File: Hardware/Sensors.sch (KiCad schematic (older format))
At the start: 8 parts, among them U4 MS5611, U5 HMC5883L, U6 L3G4200D

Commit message: Roughed out PCB layout
Known issues:
- SW_PUSH holes too small. New footprint needed
- Sensor footprints are completely wrong.
- Regulator footprints might not be correct.

Tasks:
- Place passives according to schematic (especially
  with decoupling capacitors.
- Condense layout as much as possible for
  smallest board size
- Route board
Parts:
- C15, C16, C3, C4: footprint (none) -> Capacitors_SMD:C_0805_HandSoldering
- R6: footprint (none) -> Resistors_SMD:R_0805_HandSoldering
- U4: footprint (none) -> SON:SON125P500X300-8N
- U5, U6: footprint (none) -> Housings_SSOP:SSOP-16_4.4x5.2mm_Pitch0.65mm
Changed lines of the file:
@@
 F 0 "U5" H 4050 3650 60  0000 C CNN
 F 1 "HMC5883L" H 4050 3450 60  0000 C CNN
-F 2 "" H 4200 3350 60  0000 C CNN
+F 2 "Housings_SSOP:SSOP-16_4.4x5.2mm_Pitch0.65mm" H 4200 3350 60  0001 C CNN
 F 3 "" H 4200 3350 60  0000 C CNN
 	1    4050 3550
@@
 F 0 "U4" H 2200 4000 60  0000 C CNN
 F 1 "MS5611" H 2200 3100 60  0000 C CNN
-F 2 "" H 2200 3850 60  0000 C CNN
+F 2 "SON:SON125P500X300-8N" H 2200 3850 60  0001 C CNN
 F 3 "" H 2200 3850 60  0000 C CNN
 	1    2200 3550
@@
 F 0 "U6" H 6900 3650 60  0000 C CNN
 F 1 "L3G4200D" H 6900 3450 60  0000 C CNN
-F 2 "" H 7050 3350 60  0000 C CNN
+F 2 "Housings_SSOP:SSOP-16_4.4x5.2mm_Pitch0.65mm" H 7050 3350 60  0001 C CNN
 F 3 "" H 7050 3350 60  0000 C CNN
 	1    6900 3550
@@
 F 0 "C4" H 4900 4200 50  0000 L CNN
 F 1 "4.6uF" H 4900 4000 50  0000 L CNN
-F 2 "" H 4888 3950 30  0000 C CNN
+F 2 "Capacitors_SMD:C_0805_HandSoldering" H 4888 3950 30  0001 C CNN
 F 3 "" H 4850 4100 60  0000 C CNN
 	1    4850 4100
@@
 F 0 "C3" H 4600 4200 50  0000 L CNN
 F 1 ".22uF" H 4600 4000 50  0000 L CNN
-F 2 "" H 4588 3950 30  0000 C CNN
+F 2 "Capacitors_SMD:C_0805_HandSoldering" H 4588 3950 30  0001 C CNN
 F 3 "" H 4550 4100 60  0000 C CNN
 	1    4550 4100
@@
 F 0 "C16" H 8600 2950 50  0000 L CNN
 F 1 ".47uF" H 8600 2750 50  0000 L CNN
-F 2 "" H 8588 2700 30  0000 C CNN
+F 2 "Capacitors_SMD:C_0805_HandSoldering" H 8588 2700 30  0001 C CNN
 F 3 "" H 8550 2850 60  0000 C CNN
 	1    8550 2850
@@
 F 0 "C15" H 8350 2550 50  0000 L CNN
 F 1 ".01uF" H 8350 2350 50  0000 L CNN
-F 2 "" H 8338 2300 30  0000 C CNN
+F 2 "Capacitors_SMD:C_0805_HandSoldering" H 8338 2300 30  0001 C CNN
 F 3 "" H 8300 2450 60  0000 C CNN
 	1    8300 2450
@@
 F 0 "R6" V 8130 2850 50  0000 C CNN
 F 1 "10K" V 8057 2851 50  0000 C CNN
-F 2 "" V 7980 2850 30  0000 C CNN
+F 2 "Resistors_SMD:R_0805_HandSoldering" V 7980 2850 30  0001 C CNN
 F 3 "" H 8050 2850 30  0000 C CNN
 	1    8050 2850

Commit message: Began routing
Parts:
- U5: footprint Housings_SSOP:SSOP-16_4.4x5.2mm_Pitch0.65mm -> PQFN:PQFN50P300X300-16N-EXTENDED
- U6: footprint Housings_SSOP:SSOP-16_4.4x5.2mm_Pitch0.65mm -> PQFN:PQFN65P400X400-16N-EXTENDED
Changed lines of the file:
@@
 F 0 "U5" H 4050 3650 60  0000 C CNN
 F 1 "HMC5883L" H 4050 3450 60  0000 C CNN
-F 2 "Housings_SSOP:SSOP-16_4.4x5.2mm_Pitch0.65mm" H 4200 3350 60  0001 C CNN
+F 2 "PQFN:PQFN50P300X300-16N-EXTENDED" H 4200 3350 60  0001 C CNN
 F 3 "" H 4200 3350 60  0000 C CNN
 	1    4050 3550
@@
 F 0 "U6" H 6900 3650 60  0000 C CNN
 F 1 "L3G4200D" H 6900 3450 60  0000 C CNN
-F 2 "Housings_SSOP:SSOP-16_4.4x5.2mm_Pitch0.65mm" H 7050 3350 60  0001 C CNN
+F 2 "PQFN:PQFN65P400X400-16N-EXTENDED" H 7050 3350 60  0001 C CNN
 F 3 "" H 7050 3350 60  0000 C CNN
 	1    6900 3550

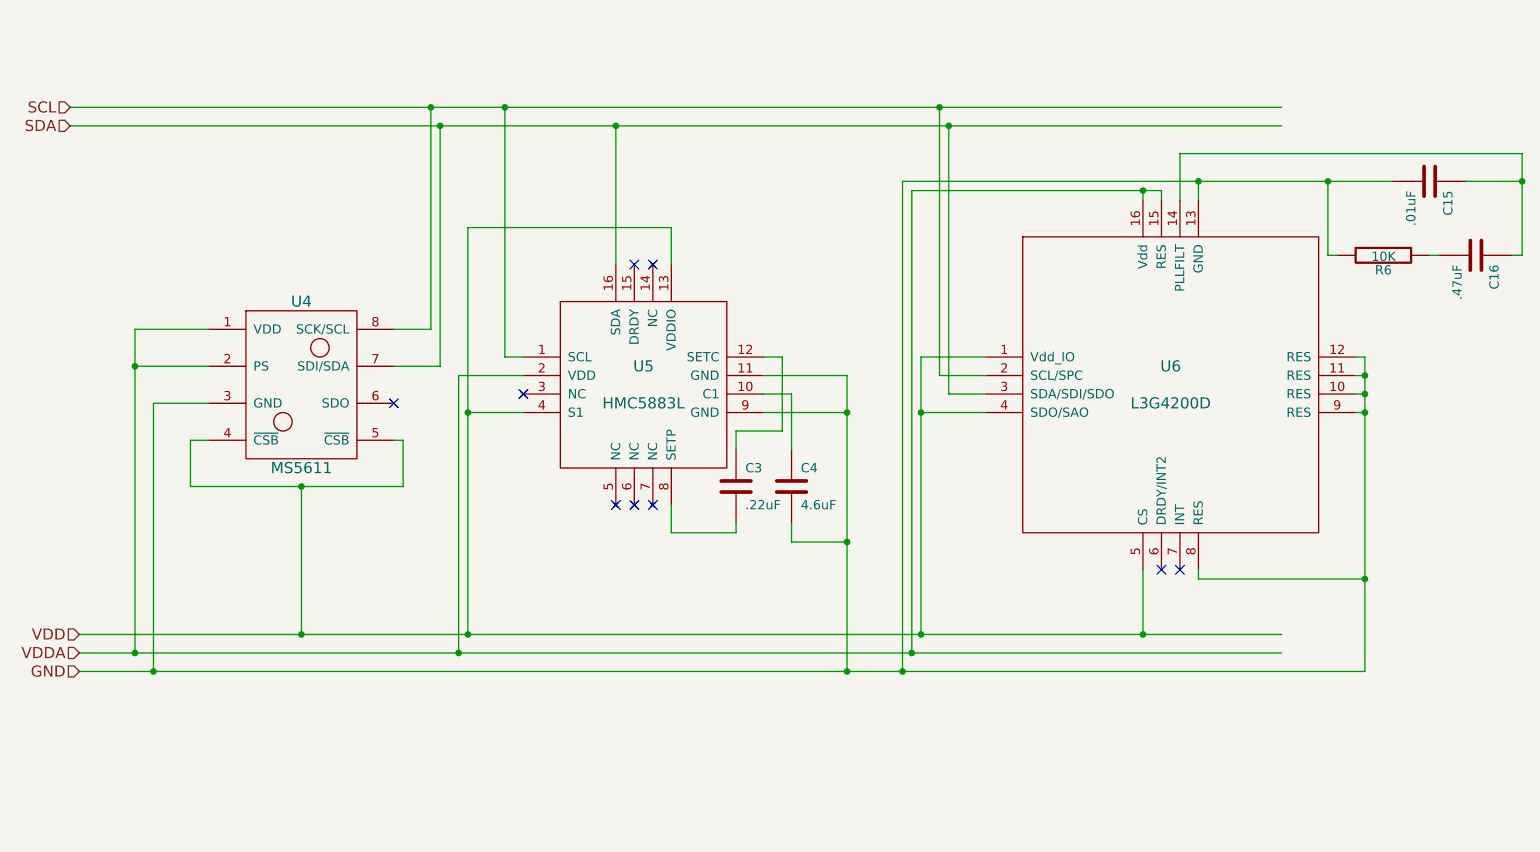
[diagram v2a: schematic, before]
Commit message: Finished schematic work. Began footprints
Began assigning footprints for R2
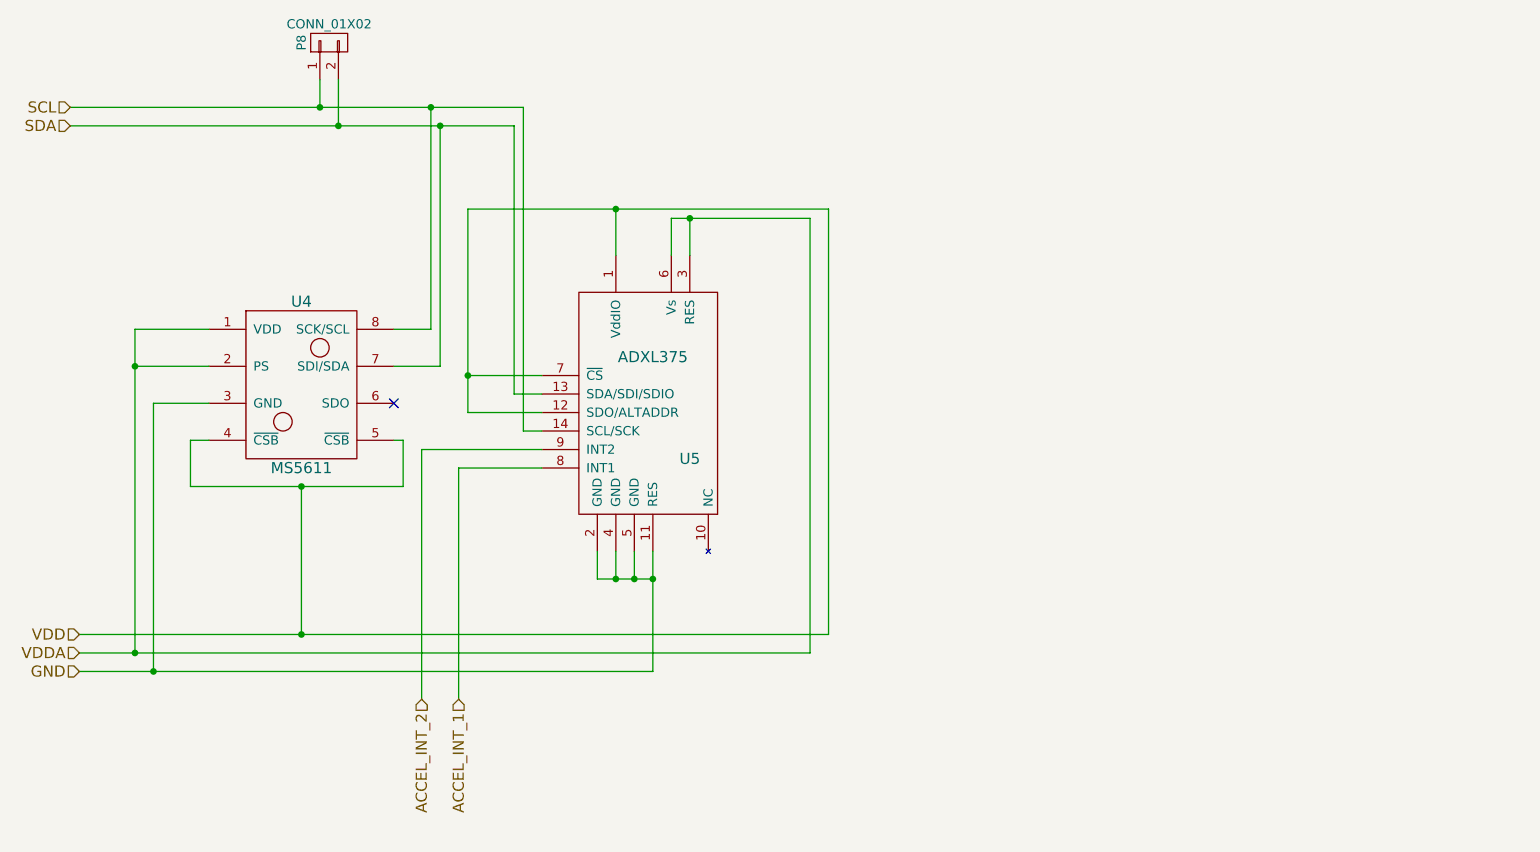
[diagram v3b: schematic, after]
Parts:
- removed C15: .01uF, Capacitors_SMD:C_0805_HandSoldering, symbol C
- removed C16: .47uF, Capacitors_SMD:C_0805_HandSoldering, symbol C
- removed C3: .22uF, Capacitors_SMD:C_0805_HandSoldering, symbol C
- removed C4: 4.6uF, Capacitors_SMD:C_0805_HandSoldering, symbol C
- removed R6: 10K, Resistors_SMD:R_0805_HandSoldering, symbol R
- removed U5: HMC5883L, PQFN:PQFN50P300X300-16N-EXTENDED, symbol HMC5883L
- removed U6: L3G4200D, PQFN:PQFN65P400X400-16N-EXTENDED, symbol L3G4200D
- added P8: CONN_01X02, Socket_Strips:Socket_Strip_Straight_2x01, symbol CONN_01X02
- added U5: ADXL375, PQFN:PQFN50P300X300-16N-EXTENDED, symbol ADXL375
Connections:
- net labels added: ACCEL_INT_1, ACCEL_INT_2
- wire segments 73 -> 45
- no-connect marks 9 -> 1

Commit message: Finished creating footprints
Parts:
- U4: footprint SON:SON125P500X300-8N -> Local:MS5611-EXT
- U5: footprint PQFN:PQFN50P300X300-16N-EXTENDED -> Local:ADXL375-EXT
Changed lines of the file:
@@
 F 0 "U4" H 2200 4000 60  0000 C CNN
 F 1 "MS5611" H 2200 3100 60  0000 C CNN
-F 2 "SON:SON125P500X300-8N" H 2200 3850 60  0001 C CNN
+F 2 "Local:MS5611-EXT" H 2200 3850 60  0001 C CNN
 F 3 "" H 2200 3850 60  0000 C CNN
 	1    2200 3550
@@
 F 0 "U5" H 4300 3250 60  0000 C CNN
 F 1 "ADXL375" H 4100 3800 60  0000 C CNN
-F 2 "PQFN:PQFN50P300X300-16N-EXTENDED" H 4100 3600 60  0001 C CNN
+F 2 "Local:ADXL375-EXT" H 4100 3600 60  0001 C CNN
 F 3 "" H 4100 3600 60  0000 C CNN
 	1    4100 3600
